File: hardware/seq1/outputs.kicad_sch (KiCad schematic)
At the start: 18 parts, among them J1 AudioJack2_SwitchT, J2 AudioJack2_SwitchT, J4 AudioJack2_SwitchT, U6 TL074

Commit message: schematic and layout for v1 board
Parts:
- added C5: 220p, Capacitor_THT:C_Disc_D5.0mm_W2.5mm_P5.00mm, symbol Device:C
- added J5: AudioJack2_SwitchT, Connector_Audio_Custom:Mono_Jack_3.5mm_THT_Horizontal, symbol Connector_Audio:AudioJack2_SwitchT
- added Q1: 2N3904, Package_TO_SOT_THT:TO-92_Inline, symbol Transistor_BJT:2N3904
- added R14, R15, R18: 10k, Resistor_THT:R_Axial_DIN0207_L6.3mm_D2.5mm_P2.54mm_Vertical, symbol Device:R_US
- added R16: 1k, Resistor_THT:R_Axial_DIN0207_L6.3mm_D2.5mm_P2.54mm_Vertical, symbol Device:R_US
- added R17: 100k, Resistor_THT:R_Axial_DIN0207_L6.3mm_D2.5mm_P2.54mm_Vertical, symbol Device:R_US
- added RV11: 50k, Potentiometer_THT:Potentiometer_Bourns_3296W_Vertical, symbol Device:R_Potentiometer_US
- C12, C13: value 100p -> 220p
- R12, R13: value 20k -> 10k
- R5: footprint (none) -> Resistor_THT:R_Axial_DIN0207_L6.3mm_D2.5mm_P10.16mm_Horizontal
- R8: footprint (none) -> Resistor_THT:R_Axial_DIN0207_L6.3mm_D2.5mm_P2.54mm_Vertical
- R9: value 10k -> 0
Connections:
- net GATE: now also R14.2; no longer R13.2
- net GND: now also J4.S, C5.1, J5.S, J5.TN, Q1.1 (E), RV11.2, RV11.3; no longer R9.2
- net at R8.1: now also R11.1, U6.7; no longer J2.T
- net at R10.1: now also U6.3 (+); no longer U6.12 (+)
- net at R5.1: now also R6.1, U6.14; no longer J1.T
- net at C12.2, R12.1: now also U6.12 (+); no longer U6.3 (+)
- net at R6.2, RV9.1: now also U6.13 (-); no longer U6.2 (-)
- net at U6.10 (+): now also C5.2, R14.1; no longer R9.1
- net at U6.9 (-): now also R15.2, RV11.1; no longer U6.8
- net SYNC_OUT_O: now reaches J4.T
- net SYNC_OUT_O: now also R8.2
- new net: Q1.2 (B), R17.1
- new net: J5.T, R17.2
- new net: R15.1, R16.1, U6.8
- new net: R9.1, U6.1
- new net: R9.2, U6.2 (-)
- new net +3V3: R18.1
- new net CV_O: J1.T, R5.2
- new net GATE_O: J2.T, R16.2
- new net SYNC_IN: Q1.3 (C), R18.2
- new net SYNC_OUT: R13.2
- no-connect marks 0 -> 3
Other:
- note added: "SYNC IN 0-5V"
- note added: "SYNC OUT 0-5V"
- moved on the sheet: C10, C11, C12, C13, J1, J2, J4, R10, R11, R12, R13, R5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

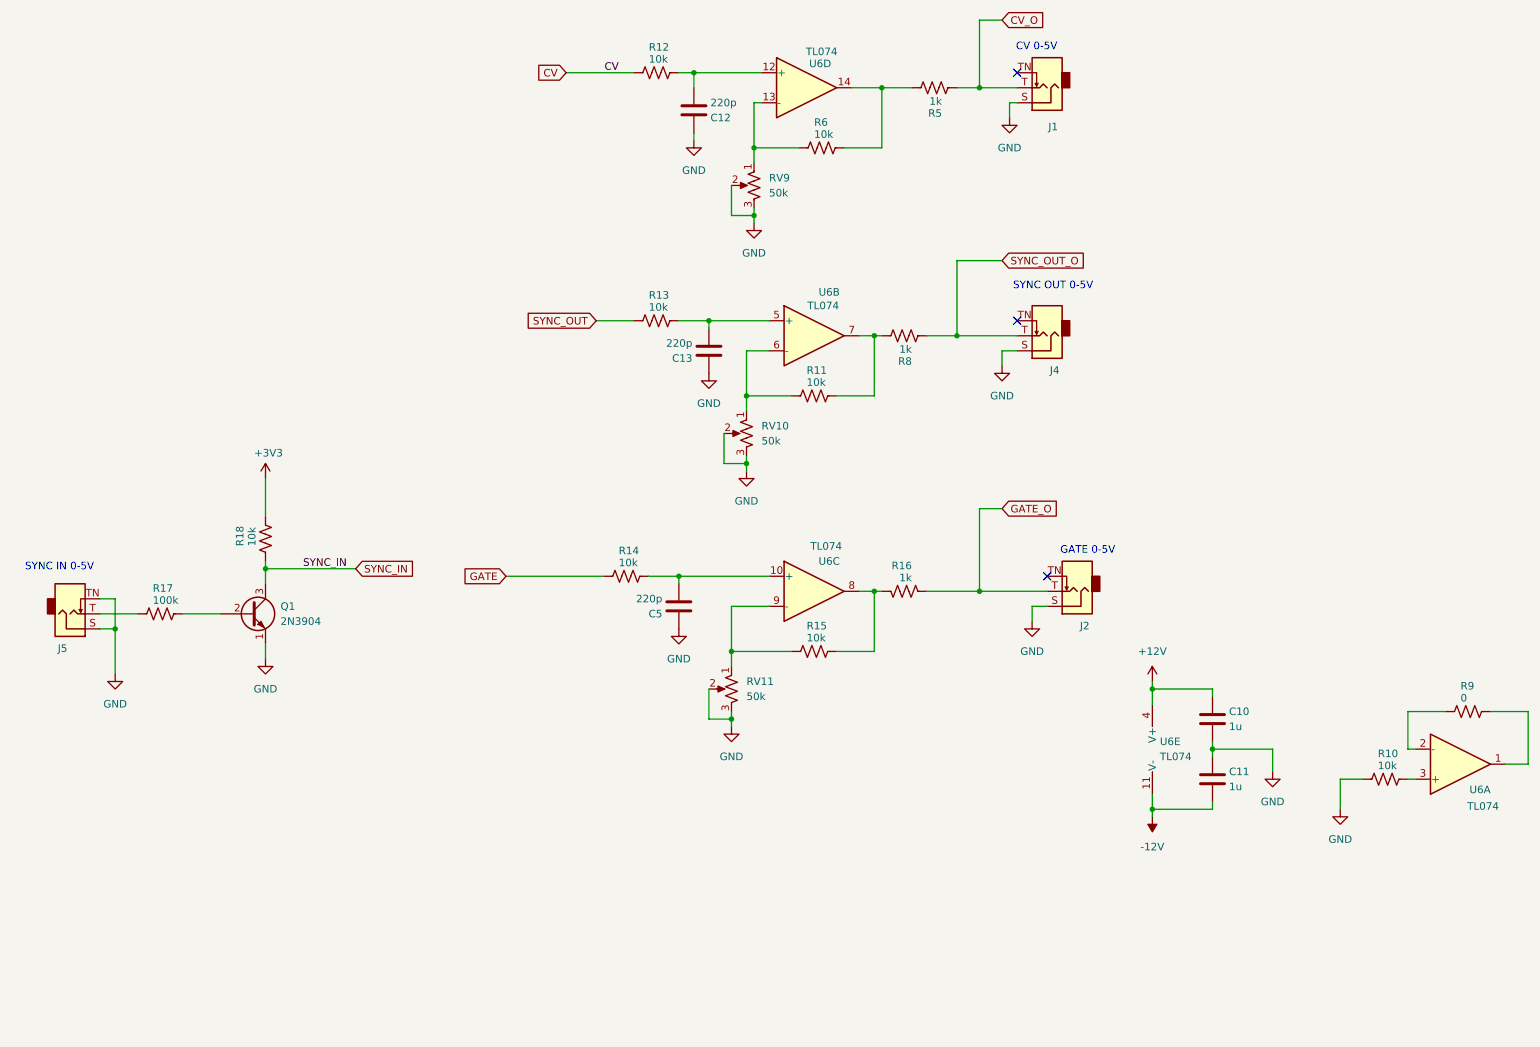
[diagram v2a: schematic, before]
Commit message: updating the board with new line in
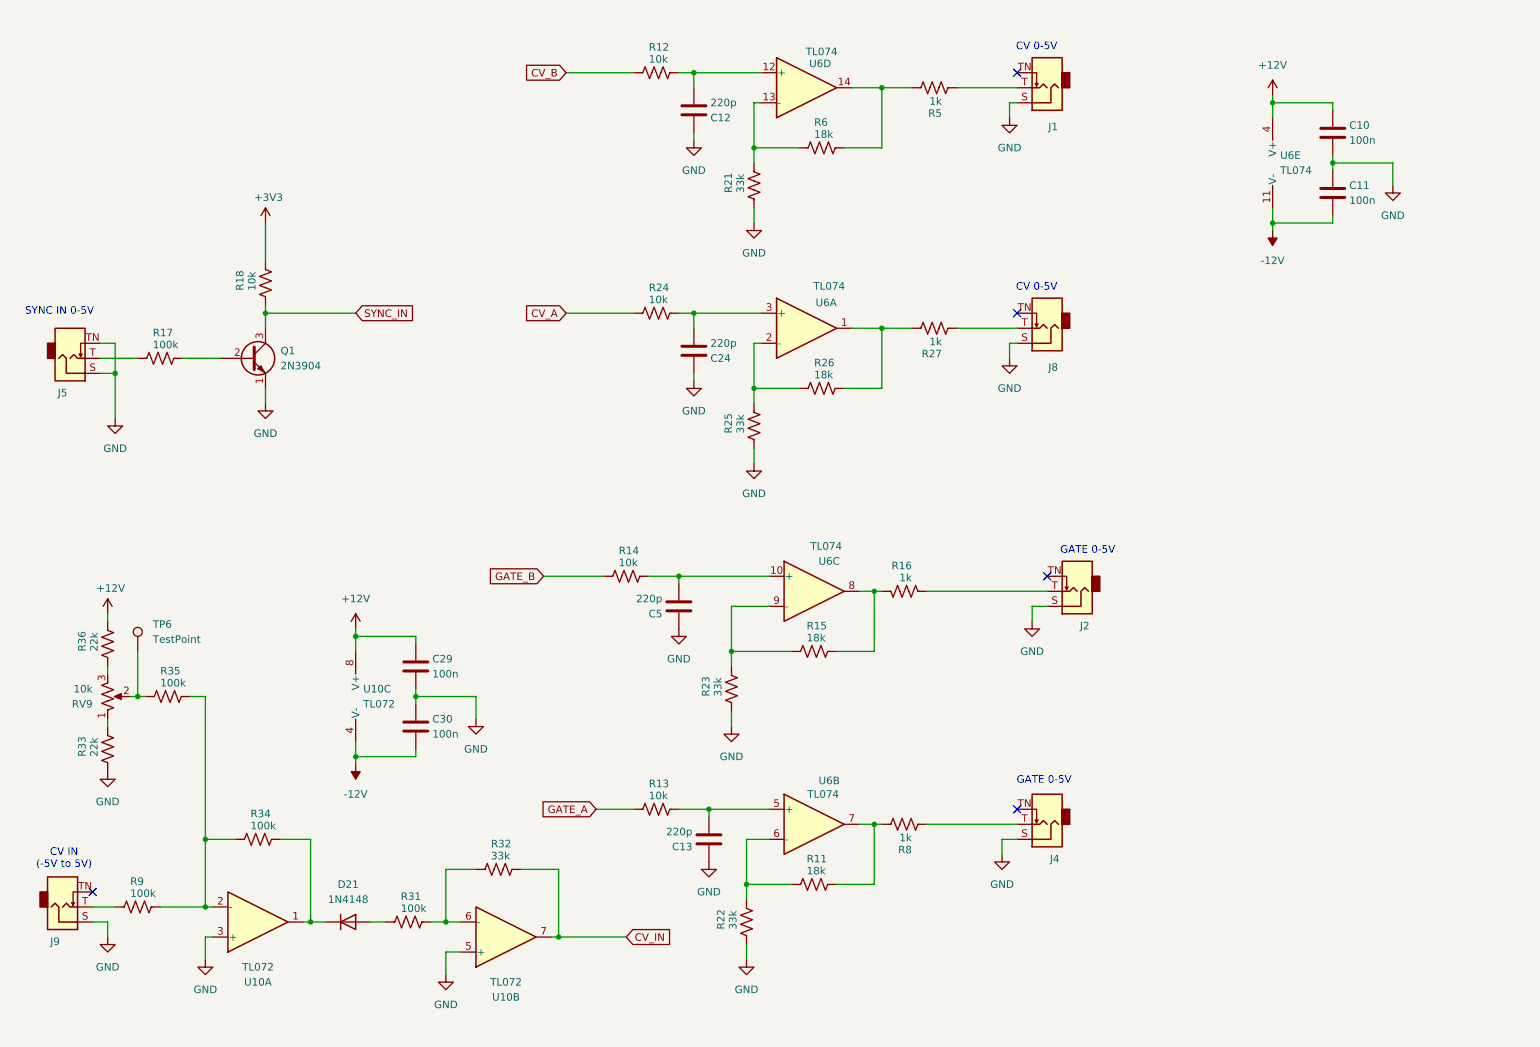
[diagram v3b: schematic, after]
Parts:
- removed R10: 10k, Resistor_THT:R_Axial_DIN0207_L6.3mm_D2.5mm_P2.54mm_Vertical, symbol Device:R_US
- removed RV10, RV11: 50k, Potentiometer_THT:Potentiometer_Bourns_3296W_Vertical, symbol Device:R_Potentiometer_US
- added C24: 220p, Capacitor_THT:C_Disc_D5.0mm_W2.5mm_P2.50mm, symbol Device:C
- added C29, C30: 100n, Capacitor_THT:C_Disc_D5.0mm_W2.5mm_P2.50mm, symbol Device:C
- added D21: 1N4148, Diode_THT:D_DO-35_SOD27_P2.54mm_Vertical_AnodeUp, symbol Diode:1N4148
- added J8, J9: AudioJack2_SwitchT, Audio_Jacks:Jack_3.5mm_QingPu_WQP-PJ301M-12_Vertical, symbol Connector_Audio:AudioJack2_SwitchT
- added R21, R22, R23, R25, R32: 33k, Resistor_THT:R_Axial_DIN0204_L3.6mm_D1.6mm_P2.54mm_Vertical, symbol Device:R_US
- added R24: 10k, Resistor_THT:R_Axial_DIN0204_L3.6mm_D1.6mm_P2.54mm_Vertical, symbol Device:R_US
- added R26: 18k, Resistor_THT:R_Axial_DIN0204_L3.6mm_D1.6mm_P2.54mm_Vertical, symbol Device:R_US
- added R27: 1k, Resistor_THT:R_Axial_DIN0204_L3.6mm_D1.6mm_P7.62mm_Horizontal, symbol Device:R_US
- added R31: 100k, Resistor_THT:R_Axial_DIN0204_L3.6mm_D1.6mm_P7.62mm_Horizontal, symbol Device:R_US
- added R33, R36: 22k, Resistor_THT:R_Axial_DIN0204_L3.6mm_D1.6mm_P2.54mm_Vertical, symbol Device:R_US
- added R34, R35: 100k, Resistor_THT:R_Axial_DIN0204_L3.6mm_D1.6mm_P2.54mm_Vertical, symbol Device:R_US
- added TP6: TestPoint, Connector_PinHeader_2.54mm:PinHeader_1x01_P2.54mm_Vertical, symbol Connector:TestPoint
- added U10: TL072, Package_DIP:DIP-8_W7.62mm_Socket, symbol Amplifier_Operational:TL072
- C10, C11: value 1u -> 100n; footprint Capacitor_THT:C_Disc_D5.0mm_W2.5mm_P5.00mm -> Capacitor_THT:C_Disc_D5.0mm_W2.5mm_P2.50mm
- C12, C13, C5: footprint Capacitor_THT:C_Disc_D5.0mm_W2.5mm_P5.00mm -> Capacitor_THT:C_Disc_D5.0mm_W2.5mm_P2.50mm
- J1, J2, J4, J5: footprint Connector_Audio_Custom:Mono_Jack_3.5mm_THT_Horizontal -> Audio_Jacks:Jack_3.5mm_QingPu_WQP-PJ301M-12_Vertical
- Q1: footprint Package_TO_SOT_THT:TO-92_Inline -> Package_TO_SOT_THT:TO-92_Inline_Wide
- R11, R15, R6: value 10k -> 18k; footprint Resistor_THT:R_Axial_DIN0207_L6.3mm_D2.5mm_P2.54mm_Vertical -> Resistor_THT:R_Axial_DIN0204_L3.6mm_D1.6mm_P2.54mm_Vertical
- R12, R16, R17, R18, R8: footprint Resistor_THT:R_Axial_DIN0207_L6.3mm_D2.5mm_P2.54mm_Vertical -> Resistor_THT:R_Axial_DIN0204_L3.6mm_D1.6mm_P2.54mm_Vertical
- R13, R14: footprint Resistor_THT:R_Axial_DIN0207_L6.3mm_D2.5mm_P2.54mm_Vertical -> Resistor_THT:R_Axial_DIN0207_L6.3mm_D2.5mm_P10.16mm_Horizontal
- R5: footprint Resistor_THT:R_Axial_DIN0207_L6.3mm_D2.5mm_P10.16mm_Horizontal -> Resistor_THT:R_Axial_DIN0204_L3.6mm_D1.6mm_P2.54mm_Vertical
- R9: value 0 -> 100k; footprint Resistor_THT:R_Axial_DIN0207_L6.3mm_D2.5mm_P2.54mm_Vertical -> Resistor_THT:R_Axial_DIN0204_L3.6mm_D1.6mm_P2.54mm_Vertical
- RV9: value 50k -> 10k; footprint Potentiometer_THT:Potentiometer_Bourns_3296W_Vertical -> Potentiometer_THT:Potentiometer_Piher_PT-6-V_Vertical
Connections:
- net +12V: now also C29.1, R36.1, U10.8 (V+)
- net -12V: now also C30.2, U10.4 (V-)
- net GND: now also C24.1, C29.2, C30.1, J8.S, J9.S, R21.2, R22.2, R23.2, R25.2, R33.2, U10.3 (+), U10.5 (+); no longer RV9.2, RV9.3
- net at R15.2, U6.9 (-): now also R23.1
- net at U6.3 (+): now also C24.2, R24.1
- net at R11.2, U6.6 (-): now also R22.1
- net at R6.2, U6.13 (-): now also R21.1; no longer RV9.1
- net at R9.1: now also R34.2, R35.1, U10.2 (-); no longer U6.1
- net at U6.2 (-): now also R25.1, R26.2; no longer R9.2
- net CV renamed CV_B
- net CV_O: no longer names the net of J1.T, R5.2
- net GATE renamed GATE_B
- net GATE_O: no longer names the net of J2.T, R16.2
- net SYNC_OUT renamed GATE_A
- net SYNC_OUT_O: no longer names the net of J4.T, R8.2
- new net: J8.T, R27.2
- new net: R31.1, R32.2, U10.6 (-)
- new net: R36.2, RV9.3
- new net: D21.1 (K), R34.1, U10.1
- new net: R33.1, RV9.1
- new net: R35.2, RV9.2, TP6.1
- new net: R26.1, R27.1, U6.1
- new net: D21.2 (A), R31.2
- new net: J9.T, R9.2
- new net CV_A: R24.2
- new net CV_IN: R32.1, U10.7
- no-connect marks 3 -> 5
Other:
- note added: "CV IN (-5V to 5V)"
- note removed: "SYNC OUT 0-5V"
- company: (none) -> idyllm
- title: (none) -> Sequencer
- moved on the sheet: C10, C11, C13, J4, J5, Q1, R11, R13, R17, R18, R8, U6B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

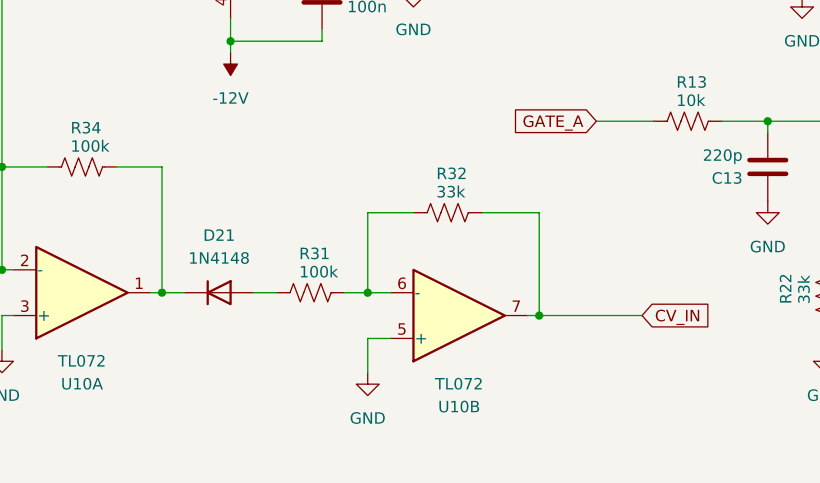
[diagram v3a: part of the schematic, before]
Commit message: layout for v2 board (WIP) with risers part of same schematic/PBC
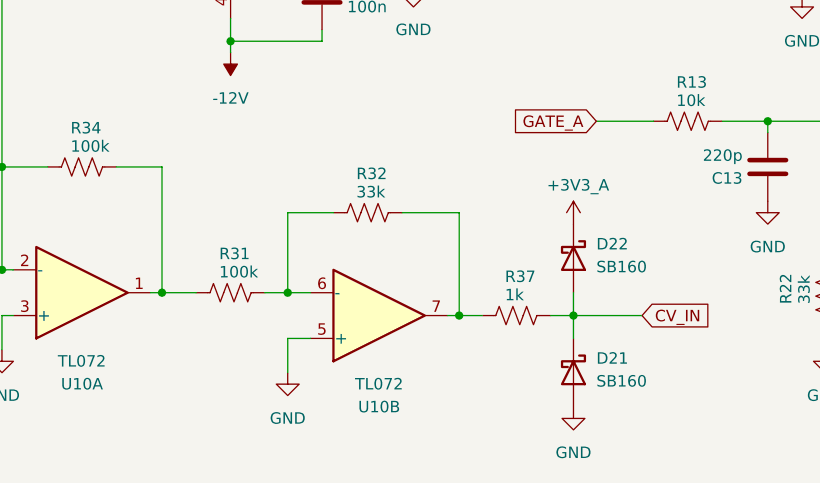
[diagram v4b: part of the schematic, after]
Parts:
- removed D21: 1N4148, Diode_THT:D_DO-35_SOD27_P2.54mm_Vertical_AnodeUp, symbol Diode:1N4148
- added D21, D22: SB160, Diode_THT:D_DO-35_SOD27_P2.54mm_Vertical_AnodeUp, symbol Diode:SB160
- added R37: 1k, Resistor_THT:R_Axial_DIN0204_L3.6mm_D1.6mm_P2.54mm_Vertical, symbol Device:R_US
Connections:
- net CV_IN: now also D21.1 (K), D22.2 (A), R37.1; no longer R32.1, U10.7
- net GND: now also D21.2 (A)
- net at R34.1, U10.1: now also R31.2
- new net: R32.1, R37.2, U10.7
- new net +3V3_A: D22.1 (K)
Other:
- moved on the sheet: R31, R32, U10B

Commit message: updated schematic title blocks for v2, generated gerbers
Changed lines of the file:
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@@
 	(title_block
 		(title "Sequencer")
-		(date "2024-10-14")
-		(rev "1.1")
+		(date "2025-11-07")
+		(rev "2.0")
 		(company "idyllm")
 		(comment 1 "CC BY-SA 4.0")
